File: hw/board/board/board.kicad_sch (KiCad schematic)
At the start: 0 parts

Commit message: Create schematic heirarchy
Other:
- added sheet board_io (board_io.kicad_sch)
- added sheet cpu (cpu.kicad_sch)
- added sheet ddr (ddr.kicad_sch)
- added sheet ethernet (ethernet.kicad_sch)
- added sheet fpga (fpga.kicad_sch)
- added sheet ftdi (ftdi.kicad_sch)
- added sheet hdmi (hdmi.kicad_sch)
- added sheet power (power.kicad_sch)
- added sheet usb (usb.kicad_sch)
- added sheet vga (vga.kicad_sch)
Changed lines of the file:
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@@
 (kicad_sch (version 20230121) (generator eeschema)
   (paper "A4")
+  (sheet (at 19.05 22.86) (size 44.45 34.29) (fields_autoplaced)
+    (stroke (width 0.1524) (type solid))
+    (fill (color 0 0 0 0.0000))
+    (property "Sheetname" "power" (at 19.05 22.1484 0)
+      (effects (font (size 1.27 1.27)) (justify left bottom))
+    )
+    (property "Sheetfile" "power.kicad_sch" (at 19.05 57.7346 0)
+      (effects (font (size 1.27 1.27)) (justify left top))
+    )
+    (instances
+      (project "board"
+        (path "/0c7bd276-5f73-4ef8-a8a2-874fce123825" (page "2"))
+      )
+    )
+  )
+  (sheet (at 210.82 71.12) (size 54.61 31.75) (fields_autoplaced)
+    (stroke (width 0.1524) (type solid))
+    (fill (color 0 0 0 0.0000))
+    (property "Sheetname" "ethernet" (at 210.82 70.4084 0)
+      (effects (font (size 1.27 1.27)) (justify left bottom))
+    )
+    (property "Sheetfile" "ethernet.kicad_sch" (at 210.82 103.4546 0)
+      (effects (font (size 1.27 1.27)) (justify left top))
+    )
+    (instances
+      (project "board"
+        (path "/0c7bd276-5f73-4ef8-a8a2-874fce123825" (page "7"))
+      )
+    )
+  )
+  (sheet (at 19.05 97.79) (size 43.18 22.86) (fields_autoplaced)
+    (stroke (width 0.1524) (type solid))
+    (fill (color 0 0 0 0.0000))
+    (property "Sheetname" "ddr" (at 19.05 97.0784 0)
+      (effects (font (size 1.27 1.27)) (justify left bottom))
+    )
+    (property "Sheetfile" "ddr.kicad_sch" (at 19.05 121.2346 0)
+      (effects (font (size 1.27 1.27)) (justify left top))
+    )
+    (instances
+      (project "board"
+        (path "/0c7bd276-5f73-4ef8-a8a2-874fce123825" (page "4"))
+      )
+    )
+  )
+  (sheet (at 19.05 154.94) (size 45.72 26.67) (fields_autoplaced)
+    (stroke (width 0.1524) (type solid))
+    (fill (color 0 0 0 0.0000))
+    (property "Sheetname" "vga" (at 19.05 154.2284 0)
+      (effects (font (size 1.27 1.27)) (justify left bottom))
+    )
+    (property "Sheetfile" "vga.kicad_sch" (at 19.05 182.1946 0)
+      (effects (font (size 1.27 1.27)) (justify left top))
+    )
+    (instances
+      (project "board"
+        (path "/0c7bd276-5f73-4ef8-a8a2-874fce123825" (page "5"))
+      )
+    )
+  )
+  (sheet (at 90.17 26.67) (size 95.25 118.11) (fields_autoplaced)
+    (stroke (width 0.1524) (type solid))
+    (fill (color 0 0 0 0.0000))
+    (property "Sheetname" "fpga" (at 90.17 25.9584 0)
+      (effects (font (size 1.27 1.27)) (justify left bottom))
+    )
+    (property "Sheetfile" "fpga.kicad_sch" (at 90.17 145.3646 0)
+      (effects (font (size 1.27 1.27)) (justify left top))
+    )
+    (instances
+      (project "board"
+        (path "/0c7bd276-5f73-4ef8-a8a2-874fce123825" (page "9"))
+      )
+    )
+  )
+  (sheet (at 20.32 127) (size 43.18 17.78) (fields_autoplaced)
+    (stroke (width 0.1524) (type solid))
+    (fill (color 0 0 0 0.0000))
+    (property "Sheetname" "usb" (at 20.32 126.2884 0)
+      (effects (font (size 1.27 1.27)) (justify left bottom))
+    )
+    (property "Sheetfile" "usb.kicad_sch" (at 20.32 145.3646 0)
+      (effects (font (size 1.27 1.27)) (justify left top))
+    )
+    (instances
+      (project "board"
+        (path "/0c7bd276-5f73-4ef8-a8a2-874fce123825" (page "11"))
+      )
+    )
+  )
+  (sheet (at 205.74 24.13) (size 52.07 15.24) (fields_autoplaced)
+    (stroke (width 0.1524) (type solid))
+    (fill (color 0 0 0 0.0000))
+    (property "Sheetname" "ftdi" (at 205.74 23.4184 0)
+      (effects (font (size 1.27 1.27)) (justify left bottom))
+    )
+    (property "Sheetfile" "ftdi.kicad_sch" (at 205.74 39.9546 0)
+      (effects (font (size 1.27 1.27)) (justify left top))
+    )
+    (instances
+      (project "board"
+        (path "/0c7bd276-5f73-4ef8-a8a2-874fce123825" (page "10"))
+      )
+    )
+  )
+  (sheet (at 212.09 116.84) (size 52.07 29.21) (fields_autoplaced)
+    (stroke (width 0.1524) (type solid))
+    (fill (color 0 0 0 0.0000))
+    (property "Sheetname" "board_io" (at 212.09 116.1284 0)
+      (effects (font (size 1.27 1.27)) (justify left bottom))
+    )
+    (property "Sheetfile" "board_io.kicad_sch" (at 212.09 146.6346 0)
+      (effects (font (size 1.27 1.27)) (justify left top))
+    )
+    (instances
+      (project "board"
+        (path "/0c7bd276-5f73-4ef8-a8a2-874fce123825" (page "8"))
+      )
+    )
+  )
+  (sheet (at 19.05 67.31) (size 45.72 21.59) (fields_autoplaced)
+    (stroke (width 0.1524) (type solid))
+    (fill (color 0 0 0 0.0000))
+    (property "Sheetname" "cpu" (at 19.05 66.5984 0)
+      (effects (font (size 1.27 1.27)) (justify left bottom))
+    )
+    (property "Sheetfile" "cpu.kicad_sch" (at 19.05 89.4846 0)
+      (effects (font (size 1.27 1.27)) (justify left top))
+    )
+    (instances
+      (project "board"
+        (path "/0c7bd276-5f73-4ef8-a8a2-874fce123825" (page "3"))
+      )
+    )
+  )
+  (sheet (at 208.28 45.72) (size 50.8 15.24) (fields_autoplaced)
+    (stroke (width 0.1524) (type solid))
+    (fill (color 0 0 0 0.0000))
+    (property "Sheetname" "hdmi" (at 208.28 45.0084 0)
+      (effects (font (size 1.27 1.27)) (justify left bottom))
+    )
+    (property "Sheetfile" "hdmi.kicad_sch" (at 208.28 61.5446 0)
+      (effects (font (size 1.27 1.27)) (justify left top))
+    )
+    (instances
+      (project "board"
+        (path "/0c7bd276-5f73-4ef8-a8a2-874fce123825" (page "6"))
+      )
+    )
+  )
   (sheet_instances
     (path "/" (page "1"))

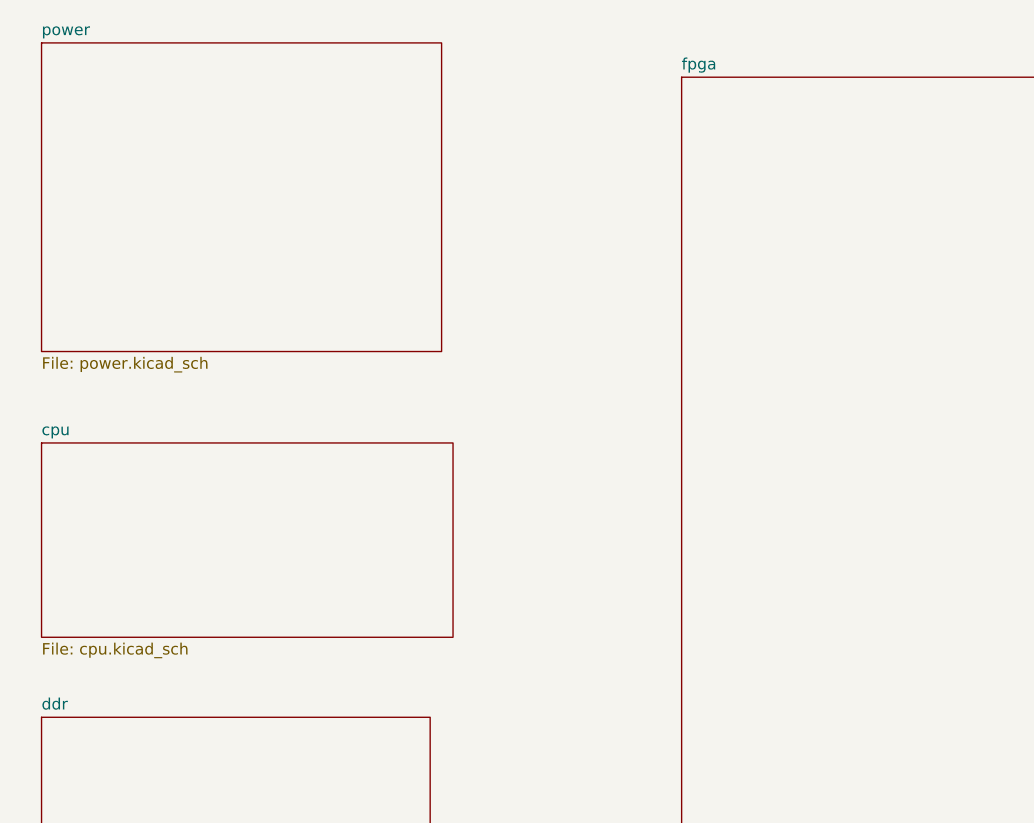
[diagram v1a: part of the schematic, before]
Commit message: Add wires to fpga block (but don't connect them)
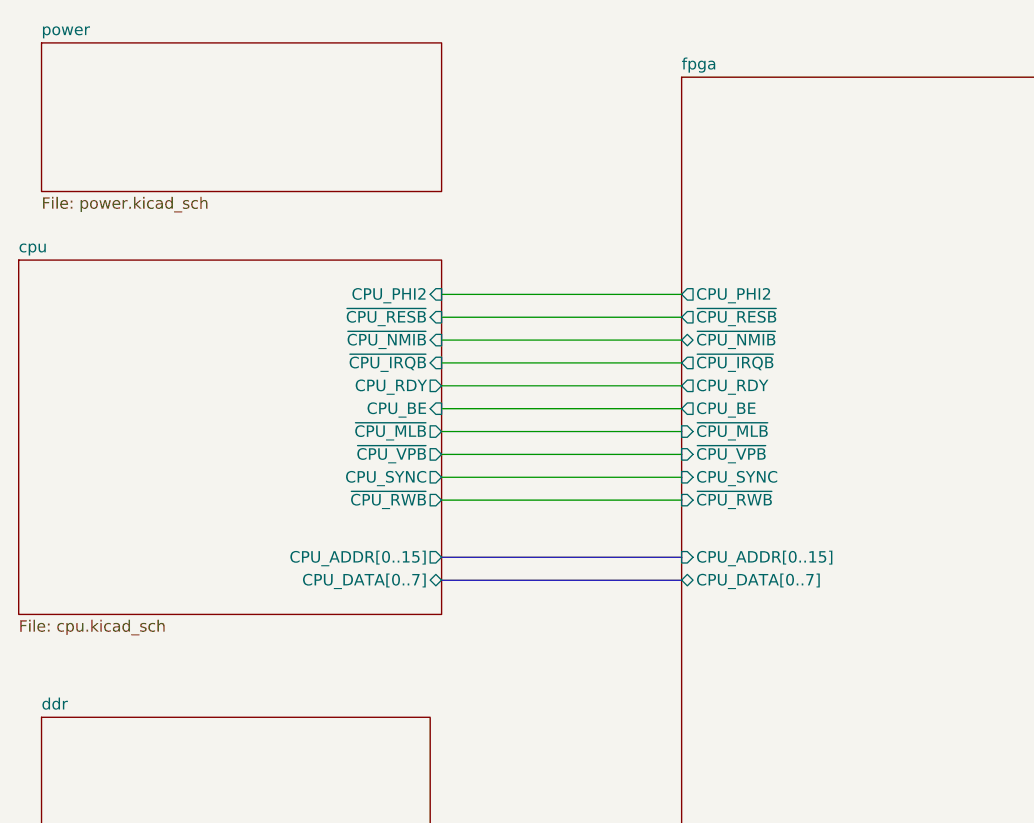
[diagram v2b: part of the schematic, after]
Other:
- sheet cpu ports: added CPU_ADDR[0..15], CPU_BE, CPU_DATA[0..7], CPU_PHI2, CPU_RDY, CPU_SYNC, ~{CPU_IRQB}, ~{CPU_MLB}, ~{CPU_NMIB}, ~{CPU_RESB}, ~{CPU_RWB}, ~{CPU_VPB}; removed none
- sheet fpga ports: added CPU_ADDR[0..15], CPU_BE, CPU_DATA[0..7], CPU_PHI2, CPU_RDY, CPU_SYNC, ~{CPU_IRQB}, ~{CPU_MLB}, ~{CPU_NMIB}, ~{CPU_RESB}, ~{CPU_RWB}, ~{CPU_VPB}; removed none
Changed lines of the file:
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@@
 (kicad_sch (version 20230121) (generator eeschema)
   (paper "A4")
-  (sheet (at 19.05 22.86) (size 44.45 34.29) (fields_autoplaced)
+  (wire (pts (xy 63.5 53.34) (xy 90.17 53.34))
+    (stroke (width 0) (type default))
+  )
+  (wire (pts (xy 63.5 55.88) (xy 90.17 55.88))
+    (stroke (width 0) (type default))
+  )
+  (wire (pts (xy 63.5 71.12) (xy 90.17 71.12))
+    (stroke (width 0) (type default))
+  )
+  (wire (pts (xy 63.5 58.42) (xy 90.17 58.42))
+    (stroke (width 0) (type default))
+  )
+  (wire (pts (xy 63.5 60.96) (xy 90.17 60.96))
+    (stroke (width 0) (type default))
+  )
+  (bus (pts (xy 63.5 80.01) (xy 90.17 80.01))
+    (stroke (width 0) (type default))
+  )
+  (wire (pts (xy 63.5 73.66) (xy 90.17 73.66))
+    (stroke (width 0) (type default))
+  )
+  (wire (pts (xy 63.5 68.58) (xy 90.17 68.58))
+    (stroke (width 0) (type default))
+  )
+  (wire (pts (xy 63.5 63.5) (xy 90.17 63.5))
+    (stroke (width 0) (type default))
+  )
+  (wire (pts (xy 63.5 50.8) (xy 90.17 50.8))
+    (stroke (width 0) (type default))
+  )
+  (wire (pts (xy 63.5 66.04) (xy 90.17 66.04))
+    (stroke (width 0) (type default))
+  )
+  (bus (pts (xy 63.5 82.55) (xy 90.17 82.55))
+    (stroke (width 0) (type default))
+  )
+  (sheet (at 19.05 22.86) (size 44.45 16.51) (fields_autoplaced)
     (stroke (width 0.1524) (type solid))
     (fill (color 0 0 0 0.0000))
@@
       (effects (font (size 1.27 1.27)) (justify left bottom))
     )
-    (property "Sheetfile" "power.kicad_sch" (at 19.05 57.7346 0)
+    (property "Sheetfile" "power.kicad_sch" (at 19.05 39.9546 0)
       (effects (font (size 1.27 1.27)) (justify left top))
     )
@@
       (effects (font (size 1.27 1.27)) (justify left top))
     )
+    (pin "CPU_ADDR[0..15]" input (at 90.17 80.01 180)
+      (effects (font (size 1.27 1.27)) (justify left))
+    )
+    (pin "CPU_DATA[0..7]" bidirectional (at 90.17 82.55 180)
+      (effects (font (size 1.27 1.27)) (justify left))
+    )
+    (pin "~{CPU_NMIB}" bidirectional (at 90.17 55.88 180)
+      (effects (font (size 1.27 1.27)) (justify left))
+    )
+    (pin "CPU_PHI2" output (at 90.17 50.8 180)
+      (effects (font (size 1.27 1.27)) (justify left))
+    )
+    (pin "~{CPU_RESB}" output (at 90.17 53.34 180)
+      (effects (font (size 1.27 1.27)) (justify left))
+    )
+    (pin "~{CPU_IRQB}" output (at 90.17 58.42 180)
+      (effects (font (size 1.27 1.27)) (justify left))
+    )
+    (pin "CPU_SYNC" input (at 90.17 71.12 180)
+      (effects (font (size 1.27 1.27)) (justify left))
+    )
+    (pin "~{CPU_MLB}" input (at 90.17 66.04 180)
+      (effects (font (size 1.27 1.27)) (justify left))
+    )
+    (pin "~{CPU_VPB}" input (at 90.17 68.58 180)
+      (effects (font (size 1.27 1.27)) (justify left))
+    )
+    (pin "~{CPU_RWB}" input (at 90.17 73.66 180)
+      (effects (font (size 1.27 1.27)) (justify left))
+    )
+    (pin "CPU_BE" output (at 90.17 63.5 180)
+      (effects (font (size 1.27 1.27)) (justify left))
+    )
+    (pin "CPU_RDY" output (at 90.17 60.96 180)
+      (effects (font (size 1.27 1.27)) (justify left))
+    )
     (instances
       (project "board"
@@
     )
   )
-  (sheet (at 19.05 67.31) (size 45.72 21.59) (fields_autoplaced)
-    (stroke (width 0.1524) (type solid))
-    (fill (color 0 0 0 0.0000))
-    (property "Sheetname" "cpu" (at 19.05 66.5984 0)
-      (effects (font (size 1.27 1.27)) (justify left bottom))
-    )
-    (property "Sheetfile" "cpu.kicad_sch" (at 19.05 89.4846 0)
-      (effects (font (size 1.27 1.27)) (justify left top))
-    )
-    (instances
+  (sheet (at 16.51 46.99) (size 46.99 39.37) (fields_autoplaced)
+    (stroke (width 0.1524) (type solid))
+    (fill (color 0 0 0 0.0000))
+    (property "Sheetname" "cpu" (at 16.51 46.2784 0)
+      (effects (font (size 1.27 1.27)) (justify left bottom))
+    )
+    (property "Sheetfile" "cpu.kicad_sch" (at 16.51 86.9446 0)
+      (effects (font (size 1.27 1.27)) (justify left top))
+    )
+    (pin "CPU_PHI2" input (at 63.5 50.8 0)
+      (effects (font (size 1.27 1.27)) (justify right))
+    )
+    (pin "CPU_ADDR[0..15]" output (at 63.5 80.01 0)
+      (effects (font (size 1.27 1.27)) (justify right))
+    )
+    (pin "~{CPU_VPB}" output (at 63.5 68.58 0)
+      (effects (font (size 1.27 1.27)) (justify right))
+    )
+    (pin "~{CPU_MLB}" output (at 63.5 66.04 0)
+      (effects (font (size 1.27 1.27)) (justify right))
+    )
+    (pin "CPU_SYNC" output (at 63.5 71.12 0)
+      (effects (font (size 1.27 1.27)) (justify right))
+    )
+    (pin "~{CPU_IRQB}" input (at 63.5 58.42 0)
+      (effects (font (size 1.27 1.27)) (justify right))
+    )
+    (pin "CPU_RDY" output (at 63.5 60.96 0)
+      (effects (font (size 1.27 1.27)) (justify right))
+    )
+    (pin "~{CPU_NMIB}" input (at 63.5 55.88 0)
+      (effects (font (size 1.27 1.27)) (justify right))
+    )
+    (pin "CPU_BE" input (at 63.5 63.5 0)
+      (effects (font (size 1.27 1.27)) (justify right))
+    )
+    (pin "~{CPU_RESB}" input (at 63.5 53.34 0)
+      (effects (font (size 1.27 1.27)) (justify right))
+    )
+    (pin "~{CPU_RWB}" output (at 63.5 73.66 0)
+      (effects (font (size 1.27 1.27)) (justify right))
+    )
+    (pin "CPU_DATA[0..7]" bidirectional (at 63.5 82.55 0)
+      (effects (font (size 1.27 1.27)) (justify right))
+    )
+    (instances

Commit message: Start work on ddr
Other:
- sheet ddr ports: added DDR_A[0..15], DDR_BA[0..2], DDR_CAS#, DDR_CK, DDR_CK#, DDR_CKE, DDR_CS#, DDR_DM, DDR_DQS, DDR_DQS#, DDR_DQ[0..7], DDR_ODT, DDR_RAS#, DDR_RESET#, DDR_WE#; removed none
- sheet fpga ports: added DDR_A[0..15], DDR_BA[0..2], DDR_CAS#, DDR_CK, DDR_CK#, DDR_CKE, DDR_CS#, DDR_DM, DDR_DQS, DDR_DQS#, DDR_DQ[0..7], DDR_ODT, DDR_RAS#, DDR_RESET#, DDR_WE#; removed none
